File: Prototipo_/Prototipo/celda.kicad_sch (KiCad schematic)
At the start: 13 parts, among them Q1 MMBT2222A, Q3 MMBT2907A, Q4 MMBT2222A

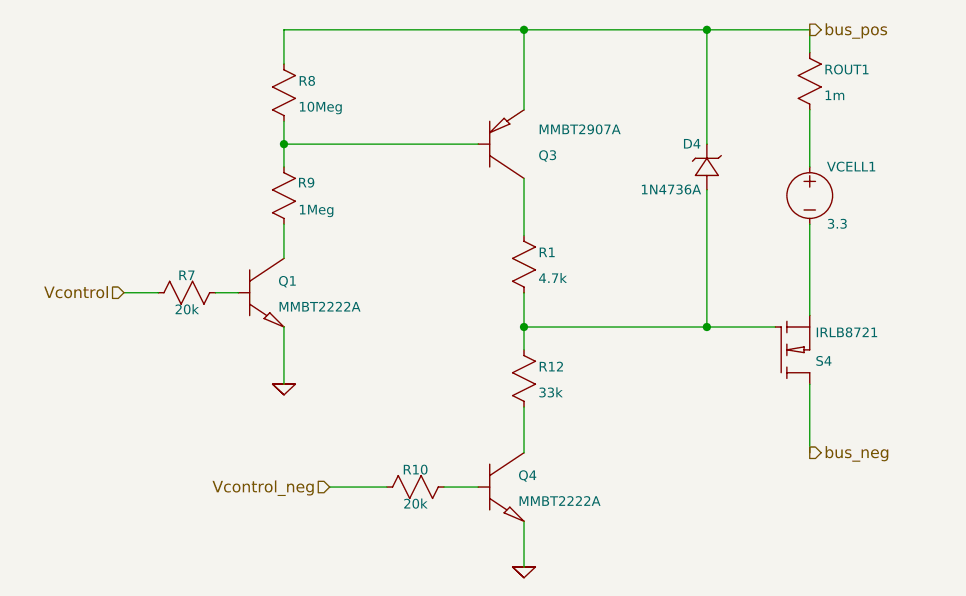
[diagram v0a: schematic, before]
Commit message: pruebo modulos de celdas en el esquematico del pcb
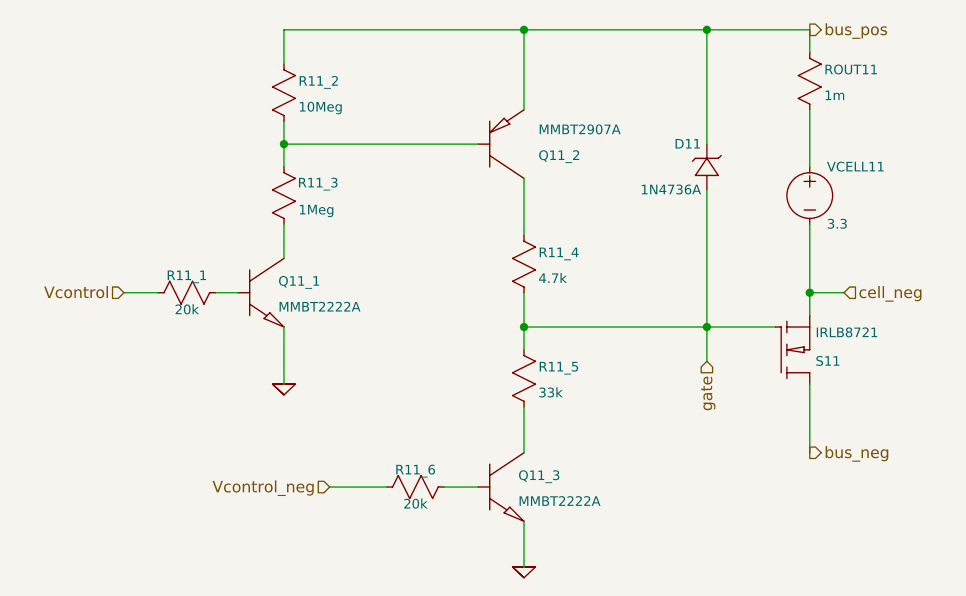
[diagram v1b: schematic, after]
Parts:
- renumbered D4 to D11, Q1 to Q11_1, Q3 to Q11_2, Q4 to Q11_3, R7 to R11_1, R8 to R11_2, R9 to R11_3, R1 to R11_4, R12 to R11_5, R10 to R11_6, ROUT1 to ROUT11, S4 to S11, VCELL1 to VCELL11
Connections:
- net gate: now reaches D11.1 (+), R11_4.2, R11_5.1, S11.1 (G)
- net cell_neg: now reaches S11.3 (S), VCELL11.2 (-)
